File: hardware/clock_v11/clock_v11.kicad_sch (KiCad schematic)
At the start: 221 parts, among them J1 RJ45, J2 Conn_01x03, J4 USB_C_Receptacle, J5 Conn_01x06_Pin, J6 Conn_01x03_Pin, J8 Conn_01x02_Pin, Q1 2N7002, Q10 2N7002, Q9 2N7002, SW1 SW_Push_4PDT, U1 ADA4807-1, U10 STM32F405RGTx, U11 AMS1117-3.3, U12 BA50DD0WHFP-TR, U13 M24C02-RMN, U14 CH340C, U15 USBLC6-2P6, U16 TLV3603DCKR, U17 SN74LVC1G14DBV, U18 TMP112AIDRLR, U19 SN74LVC1G14DBV, U2 SN74LVC1G14DBV, U20 SN74LVC1G14DBV, U21 SN74LVC1G14DBV, U23 TPS63060, U3 SN74LVC1G14DBV, U4 ADA4807-1, U5 ADA4807-1, U6 TLV3603DCKR, U7 SN74LVC1G14DBV, U8 TLV3603DCKR, U9 L78L05_SOT89, Y1 MultiOsc, Y2 16MHz

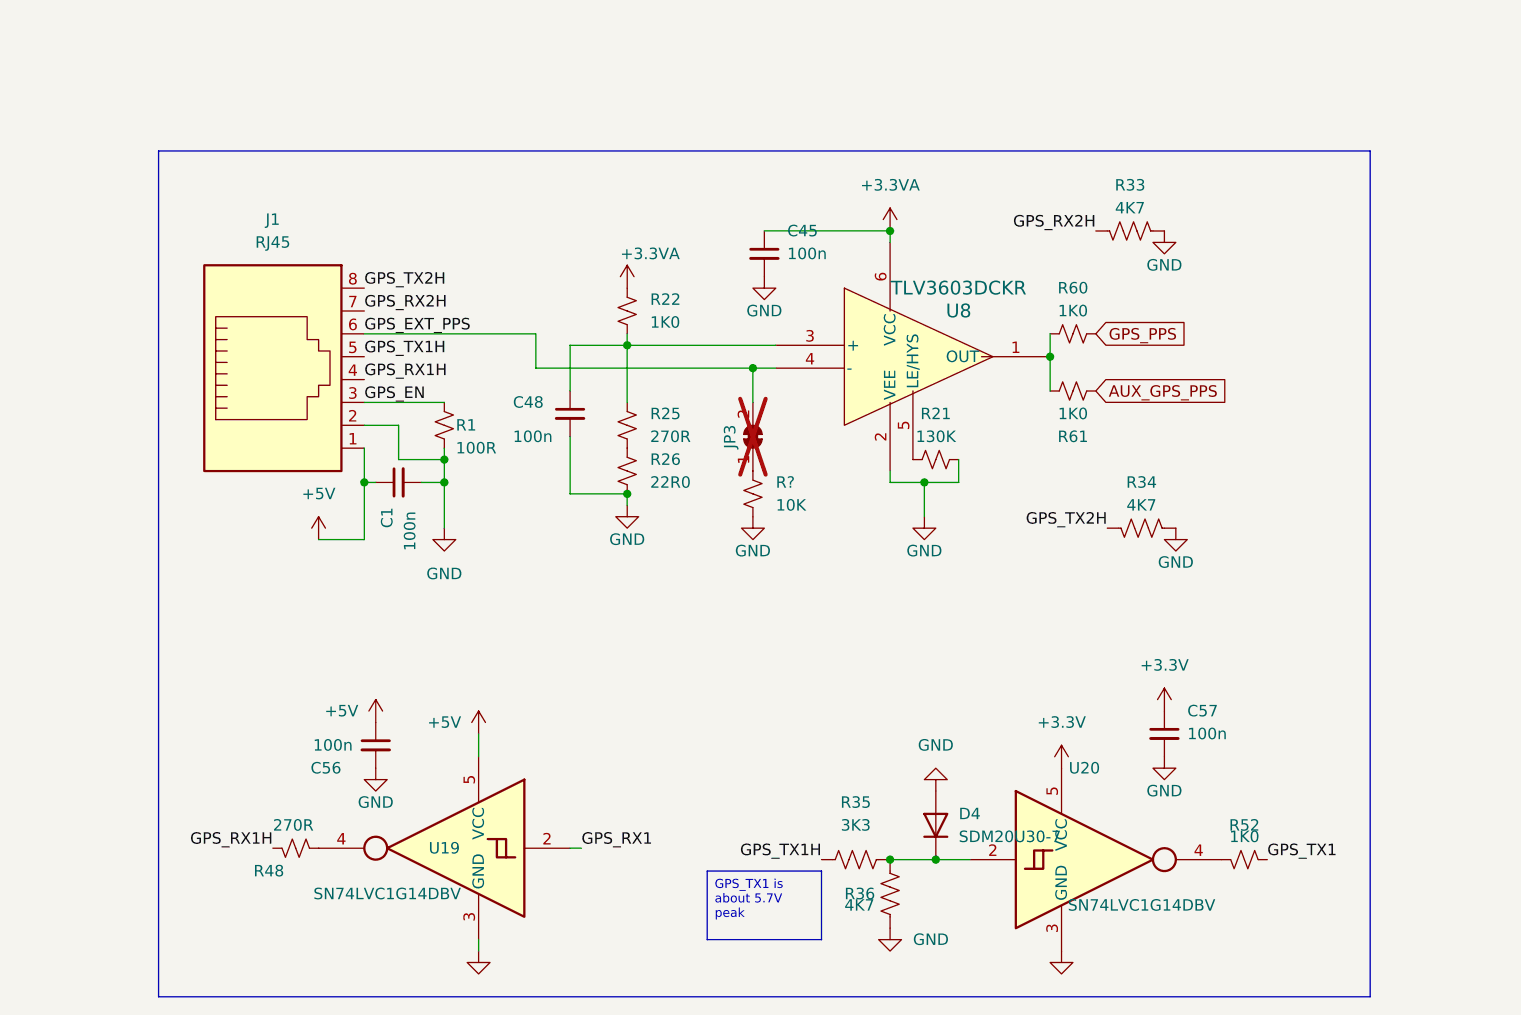
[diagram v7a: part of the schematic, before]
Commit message: add GPS hdr to clock board
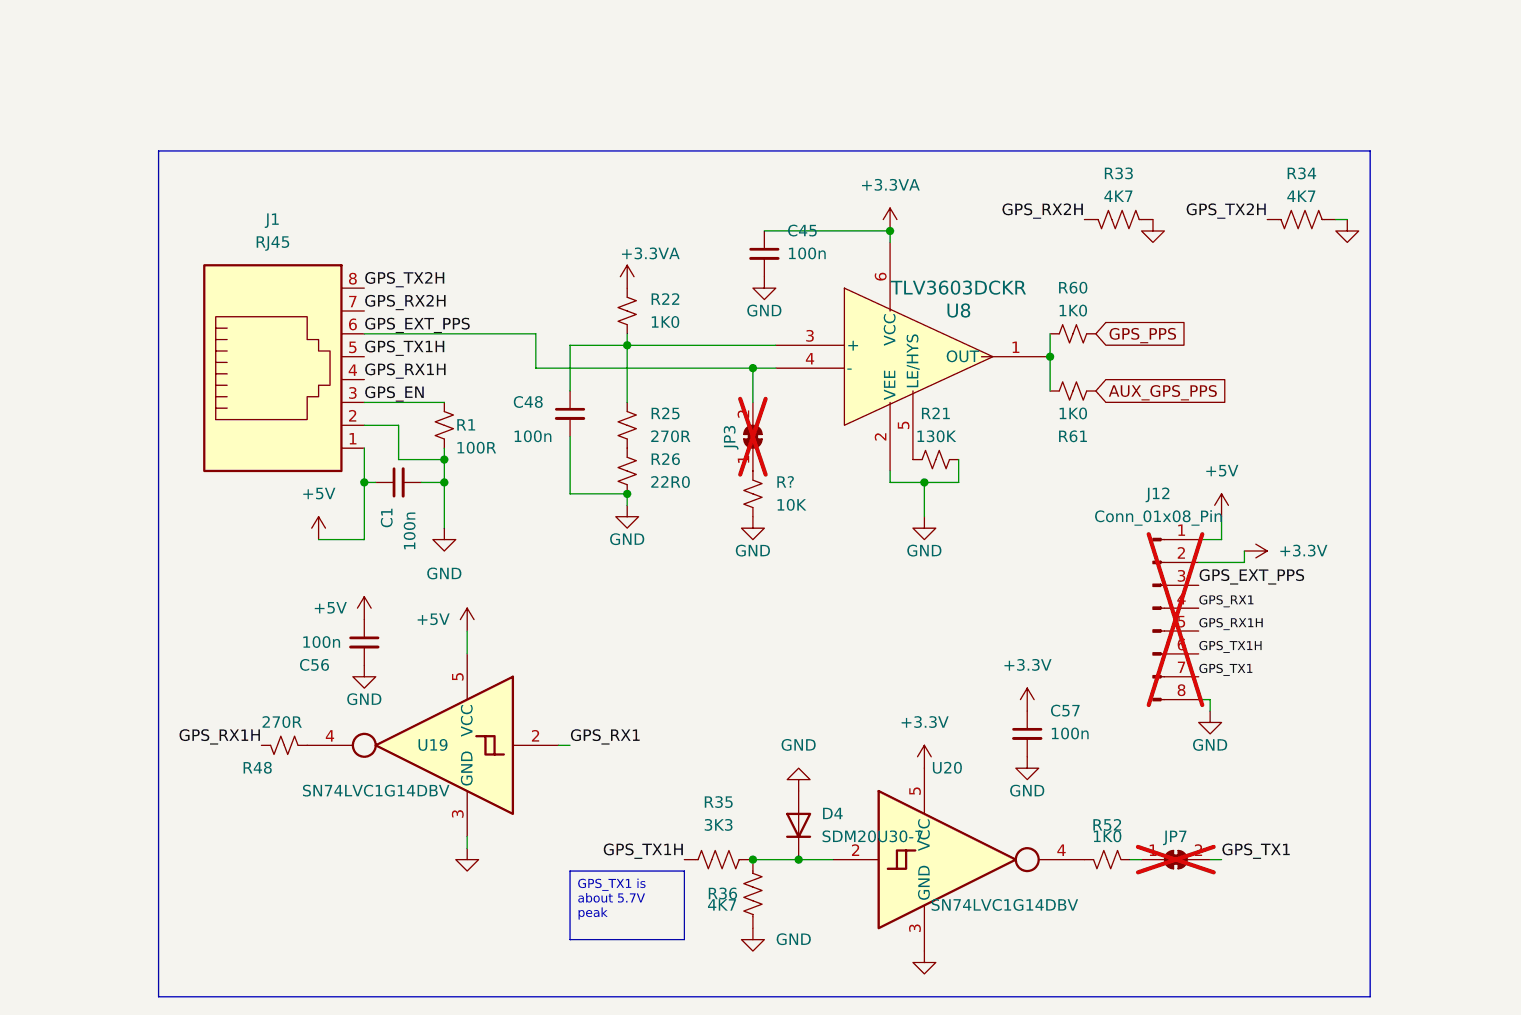
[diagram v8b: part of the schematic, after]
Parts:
- added J12: Conn_01x08_Pin, Connector_PinHeader_2.54mm:PinHeader_1x08_P2.54mm_Vertical, symbol Connector:Conn_01x08_Pin
- added JP7: SolderJumper_2_Bridged, Jumper:SolderJumper-2_P1.3mm_Bridged2Bar_RoundedPad1.0x1.5mm, symbol Jumper:SolderJumper_2_Bridged
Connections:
- net +3.3V: now also J12.2 (Pin_2)
- net +5V: now also J12.1 (Pin_1)
- net GND: now also J12.8 (Pin_8)
- net GPS_EXT_PPS: now also J12.3 (Pin_3)
- net GPS_RX1: now also J12.4 (Pin_4)
- net GPS_RX1H: now also J12.5 (Pin_5)
- net GPS_TX1: now also J12.7 (Pin_7), JP7.2 (B); no longer R52.1
- net GPS_TX1H: now also J12.6 (Pin_6)
- new net: JP7.1 (A), R52.1
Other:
- moved on the sheet: C56, C57, D4, R33, R34, R35, R36, R48, R52, U19, U20
